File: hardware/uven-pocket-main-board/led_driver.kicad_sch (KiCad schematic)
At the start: 13 parts, among them U6 SIDR392DP-T1-GE3, U7 SIDR392DP-T1-GE3, U8 TPS2HB50BQPWPRQ1

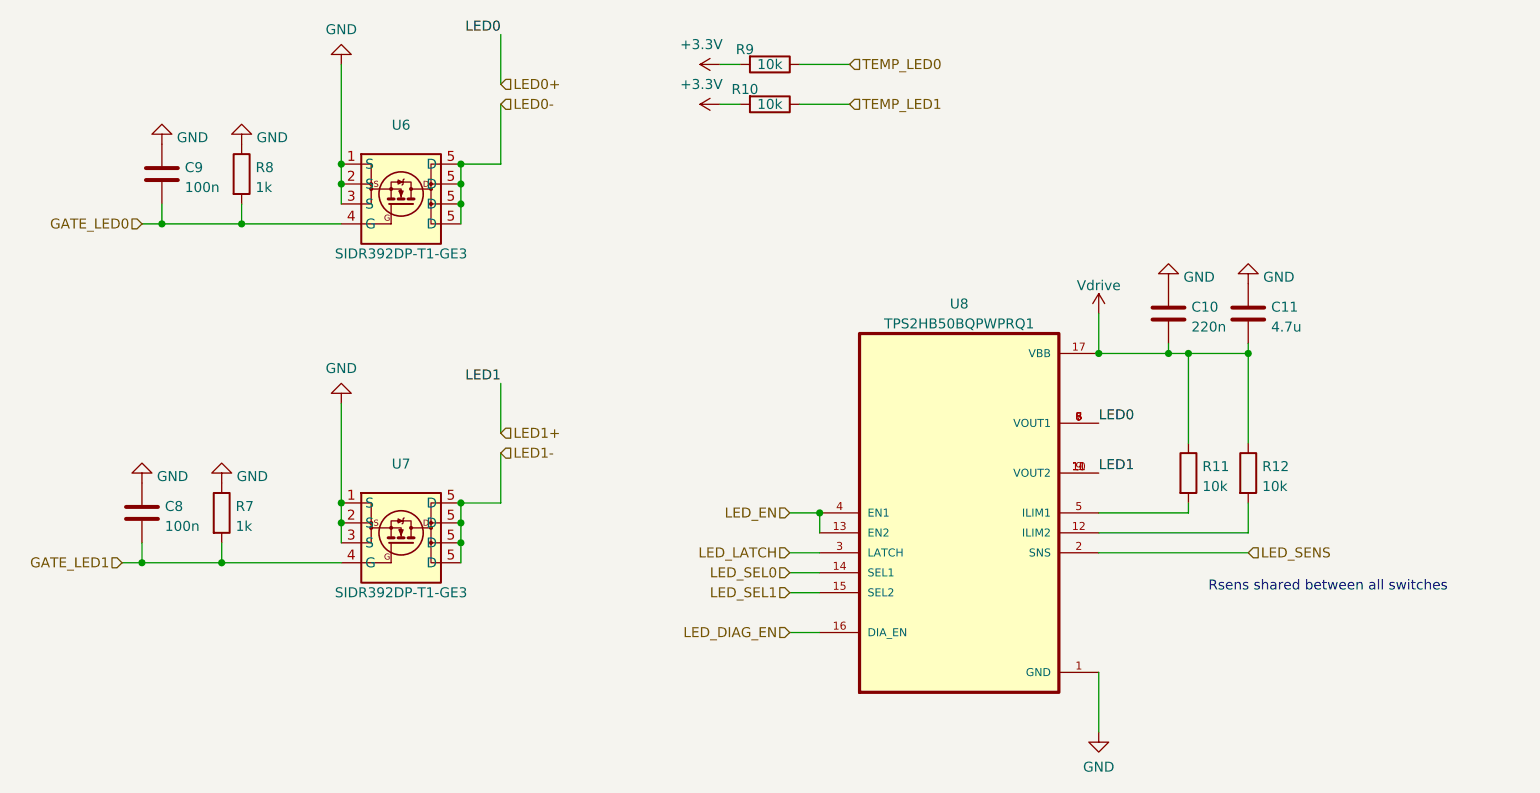
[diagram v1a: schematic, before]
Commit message: single led copper base + uven pocket finished
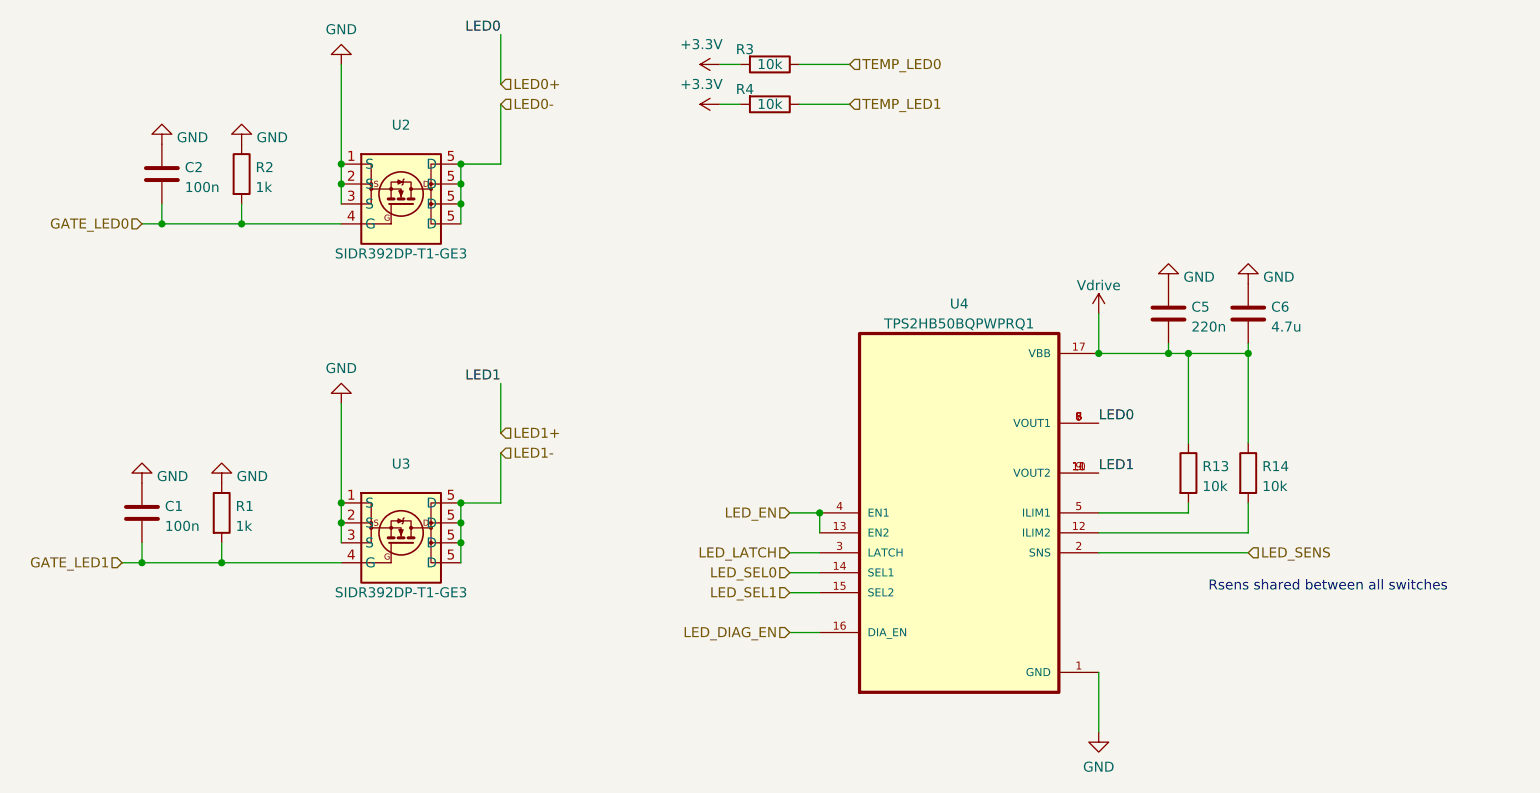
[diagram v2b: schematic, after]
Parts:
- renumbered C8 to C1, C9 to C2, C10 to C5, C11 to C6, R7 to R1, R11 to R13, R12 to R14, R8 to R2, R9 to R3, R10 to R4, U6 to U2, U7 to U3, U8 to U4
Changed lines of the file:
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@@
   (symbol (lib_id "power:GND") (at 220.98 76.2 180) (unit 1)
     (in_bom yes) (on_board yes) (fields_autoplaced)
-    (property "Reference" "#PWR0136" (id 0) (at 220.98 69.85 0)
+    (property "Reference" "#PWR0111" (id 0) (at 220.98 69.85 0)
       (effects (font (size 1.27 1.27)) hide)
     )
@@
   (symbol (lib_id "uven-mainboard-rescue:R-Device") (at 170.18 48.26 270) (unit 1)
     (in_bom yes) (on_board yes)
-    (property "Reference" "R9" (id 0) (at 167.005 46.355 90))
+    (property "Reference" "R3" (id 0) (at 167.005 46.355 90))
     (property "Value" "10k" (id 1) (at 170.18 48.26 90))
     (property "Footprint" "Resistor_SMD:R_0603_1608Metric_Pad0.98x0.95mm_HandSolder" (id 2) (at 170.18 46.482 90)
@@
   (symbol (lib_id "power:GND") (at 90.17 101.6 180) (unit 1)
     (in_bom yes) (on_board yes) (fields_autoplaced)
-    (property "Reference" "#PWR0139" (id 0) (at 90.17 95.25 0)
+    (property "Reference" "#PWR0113" (id 0) (at 90.17 95.25 0)
       (effects (font (size 1.27 1.27)) hide)
     )
@@
   (symbol (lib_id "power:GND") (at 102.87 58.42 180) (unit 1)
     (in_bom yes) (on_board yes) (fields_autoplaced)
-    (property "Reference" "#PWR0133" (id 0) (at 102.87 52.07 0)
+    (property "Reference" "#PWR0106" (id 0) (at 102.87 52.07 0)
       (effects (font (size 1.27 1.27)) hide)
     )
@@
   (symbol (lib_id "power:+3.3V") (at 163.83 48.26 90) (unit 1)
     (in_bom yes) (on_board yes)
-    (property "Reference" "#PWR0141" (id 0) (at 167.64 48.26 0)
+    (property "Reference" "#PWR0116" (id 0) (at 167.64 48.26 0)
       (effects (font (size 1.27 1.27)) hide)
     )
@@
   (symbol (lib_id "custom:SIDR392DP-T1-GE3") (at 123.19 66.04 0) (unit 1)
     (in_bom yes) (on_board yes)
-    (property "Reference" "U6" (id 0) (at 123.19 55.9902 0))
+    (property "Reference" "U2" (id 0) (at 123.19 55.9902 0))
     (property "Value" "SIDR392DP-T1-GE3" (id 1) (at 123.19 72.39 0))
     (property "Footprint" "custom_lib:PowerPAK SO-8DC" (id 2) (at 123.19 66.04 0)
@@
   (symbol (lib_id "Device:C") (at 92.71 62.23 0) (unit 1)
     (in_bom yes) (on_board yes) (fields_autoplaced)
-    (property "Reference" "C9" (id 0) (at 95.631 61.3953 0)
+    (property "Reference" "C2" (id 0) (at 95.631 61.3953 0)
       (effects (font (size 1.27 1.27)) (justify left))
     )
@@
   (symbol (lib_id "Device:C") (at 231.14 80.01 0) (unit 1)
     (in_bom yes) (on_board yes) (fields_autoplaced)
-    (property "Reference" "C11" (id 0) (at 234.061 79.1753 0)
+    (property "Reference" "C6" (id 0) (at 234.061 79.1753 0)
       (effects (font (size 1.27 1.27)) (justify left))
     )
@@
   (symbol (lib_id "Device:R") (at 223.52 100.33 0) (unit 1)
     (in_bom yes) (on_board yes) (fields_autoplaced)
-    (property "Reference" "R11" (id 0) (at 225.298 99.4953 0)
+    (property "Reference" "R13" (id 0) (at 225.298 99.4953 0)
       (effects (font (size 1.27 1.27)) (justify left))
     )
@@
   (symbol (lib_id "power:GND") (at 115.57 91.44 180) (unit 1)
     (in_bom yes) (on_board yes) (fields_autoplaced)
-    (property "Reference" "#PWR0137" (id 0) (at 115.57 85.09 0)
+    (property "Reference" "#PWR0112" (id 0) (at 115.57 85.09 0)
       (effects (font (size 1.27 1.27)) hide)
     )
@@
   (symbol (lib_id "custom:SIDR392DP-T1-GE3") (at 123.19 109.22 0) (unit 1)
     (in_bom yes) (on_board yes)
-    (property "Reference" "U7" (id 0) (at 123.19 99.1702 0))
+    (property "Reference" "U3" (id 0) (at 123.19 99.1702 0))
     (property "Value" "SIDR392DP-T1-GE3" (id 1) (at 123.19 115.57 0))
     (property "Footprint" "custom_lib:PowerPAK SO-8DC" (id 2) (at 123.19 109.22 0)
@@
   (symbol (lib_id "Device:C") (at 220.98 80.01 0) (unit 1)
     (in_bom yes) (on_board yes) (fields_autoplaced)
-    (property "Reference" "C10" (id 0) (at 223.901 79.1753 0)
+    (property "Reference" "C5" (id 0) (at 223.901 79.1753 0)
       (effects (font (size 1.27 1.27)) (justify left))
     )
@@
   (symbol (lib_id "power:Vdrive") (at 212.09 80.01 0) (unit 1)
     (in_bom yes) (on_board yes) (fields_autoplaced)
-    (property "Reference" "#PWR0140" (id 0) (at 207.01 83.82 0)
+    (property "Reference" "#PWR0115" (id 0) (at 207.01 83.82 0)
       (effects (font (size 1.27 1.27)) hide)
     )
@@
   (symbol (lib_id "Device:C") (at 90.17 105.41 0) (unit 1)
     (in_bom yes) (on_board yes) (fields_autoplaced)
-    (property "Reference" "C8" (id 0) (at 93.091 104.5753 0)
+    (property "Reference" "C1" (id 0) (at 93.091 104.5753 0)
       (effects (font (size 1.27 1.27)) (justify left))
     )
@@
   (symbol (lib_id "power:GND") (at 231.14 76.2 180) (unit 1)
     (in_bom yes) (on_board yes) (fields_autoplaced)
-    (property "Reference" "#PWR0135" (id 0) (at 231.14 69.85 0)
+    (property "Reference" "#PWR0110" (id 0) (at 231.14 69.85 0)
       (effects (font (size 1.27 1.27)) hide)
     )
@@
   (symbol (lib_id "power:GND") (at 100.33 101.6 180) (unit 1)
     (in_bom yes) (on_board yes) (fields_autoplaced)
-    (property "Reference" "#PWR0138" (id 0) (at 100.33 95.25 0)
+    (property "Reference" "#PWR0114" (id 0) (at 100.33 95.25 0)
       (effects (font (size 1.27 1.27)) hide)
     )
@@
   (symbol (lib_id "power:GND") (at 92.71 58.42 180) (unit 1)
     (in_bom yes) (on_board yes) (fields_autoplaced)
-    (property "Reference" "#PWR0132" (id 0) (at 92.71 52.07 0)
+    (property "Reference" "#PWR0108" (id 0) (at 92.71 52.07 0)
       (effects (font (size 1.27 1.27)) hide)
     )
@@
   (symbol (lib_id "power:GND") (at 115.57 48.26 180) (unit 1)
     (in_bom yes) (on_board yes) (fields_autoplaced)
-    (property "Reference" "#PWR0131" (id 0) (at 115.57 41.91 0)
+    (property "Reference" "#PWR0105" (id 0) (at 115.57 41.91 0)
       (effects (font (size 1.27 1.27)) hide)
     )
@@
   (symbol (lib_id "uven-mainboard-rescue:R-Device") (at 170.18 53.34 270) (unit 1)
     (in_bom yes) (on_board yes)
-    (property "Reference" "R10" (id 0) (at 167.005 51.435 90))
+    (property "Reference" "R4" (id 0) (at 167.005 51.435 90))
     (property "Value" "10k" (id 1) (at 170.18 53.34 90))
     (property "Footprint" "Resistor_SMD:R_0603_1608Metric_Pad0.98x0.95mm_HandSolder" (id 2) (at 170.18 51.562 90)
@@
   (symbol (lib_id "Device:R") (at 100.33 105.41 0) (unit 1)
     (in_bom yes) (on_board yes) (fields_autoplaced)
-    (property "Reference" "R7" (id 0) (at 102.108 104.5753 0)
+    (property "Reference" "R1" (id 0) (at 102.108 104.5753 0)
       (effects (font (size 1.27 1.27)) (justify left))
     )
@@
   (symbol (lib_id "TPS2HB50BQPWPRQ1:TPS2HB50BQPWPRQ1") (at 194.31 105.41 0) (unit 1)
     (in_bom yes) (on_board yes) (fields_autoplaced)
-    (property "Reference" "U8" (id 0) (at 194.31 78.7722 0))
+    (property "Reference" "U4" (id 0) (at 194.31 78.7722 0))
     (property "Value" "TPS2HB50BQPWPRQ1" (id 1) (at 194.31 81.3091 0))
     (property "Footprint" "custom_lib:SOP65P640X120-17N" (id 2) (at 194.31 105.41 0)
@@
   (symbol (lib_id "power:+3.3V") (at 163.83 53.34 90) (unit 1)
     (in_bom yes) (on_board yes)
-    (property "Reference" "#PWR0142" (id 0) (at 167.64 53.34 0)
+    (property "Reference" "#PWR0117" (id 0) (at 167.64 53.34 0)
       (effects (font (size 1.27 1.27)) hide)
     )
@@
   (symbol (lib_id "Device:R") (at 102.87 62.23 0) (unit 1)
     (in_bom yes) (on_board yes) (fields_autoplaced)
-    (property "Reference" "R8" (id 0) (at 104.648 61.3953 0)
+    (property "Reference" "R2" (id 0) (at 104.648 61.3953 0)
       (effects (font (size 1.27 1.27)) (justify left))
     )
@@
   (symbol (lib_id "Device:R") (at 231.14 100.33 0) (unit 1)
     (in_bom yes) (on_board yes) (fields_autoplaced)
-    (property "Reference" "R12" (id 0) (at 232.918 99.4953 0)
+    (property "Reference" "R14" (id 0) (at 232.918 99.4953 0)
       (effects (font (size 1.27 1.27)) (justify left))
     )
@@
   (symbol (lib_id "power:GND") (at 212.09 133.35 0) (unit 1)
     (in_bom yes) (on_board yes) (fields_autoplaced)
-    (property "Reference" "#PWR0134" (id 0) (at 212.09 139.7 0)
-      (effects (font (size 1.27 1.27)) hide)
-    )
+    (property "Reference" "#PWR0109" (id 0) (at 212.09 139.7 0)
+      (effects (font (size 1.27 1.27)) hide)
+    )
